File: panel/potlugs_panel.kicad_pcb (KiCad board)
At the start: 2 copper layers, 99 x 91 mm, 819 parts, among them J1 640456-3

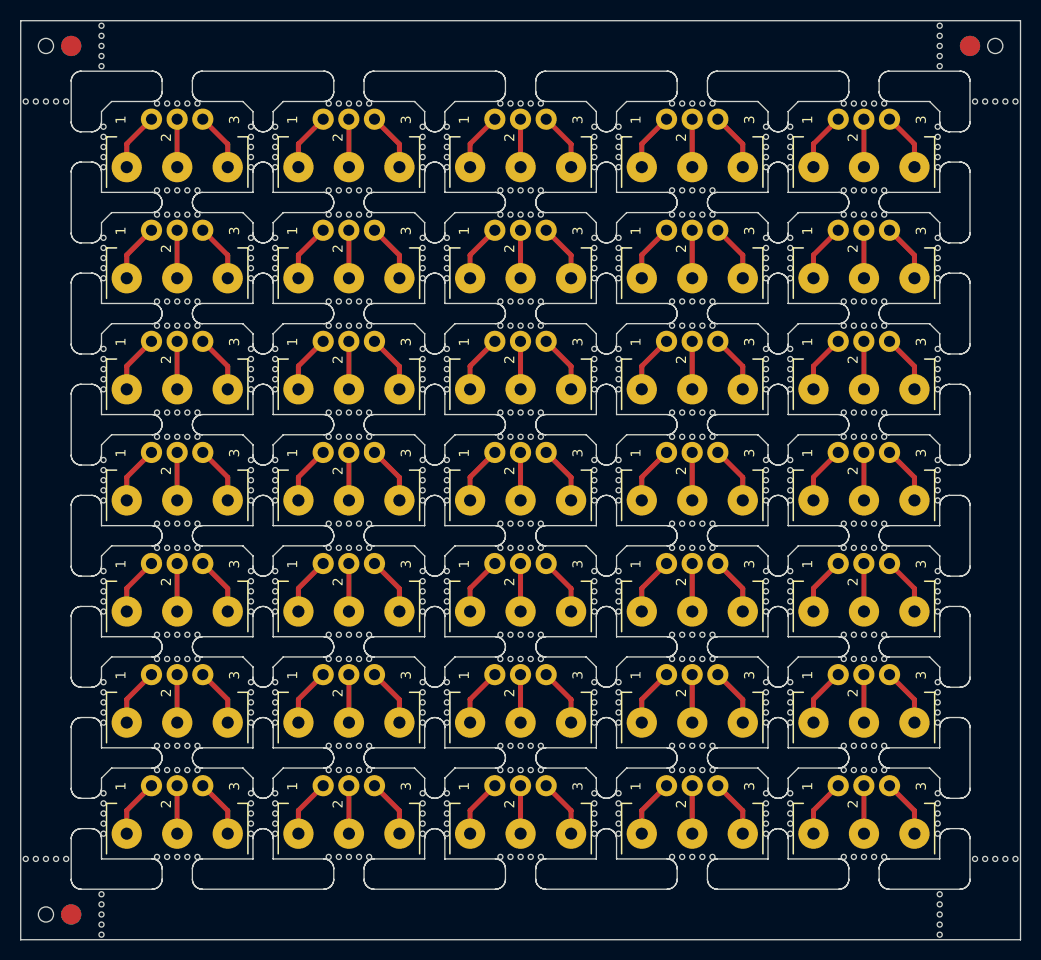
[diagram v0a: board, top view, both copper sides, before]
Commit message: Update panel layout for cost savings.
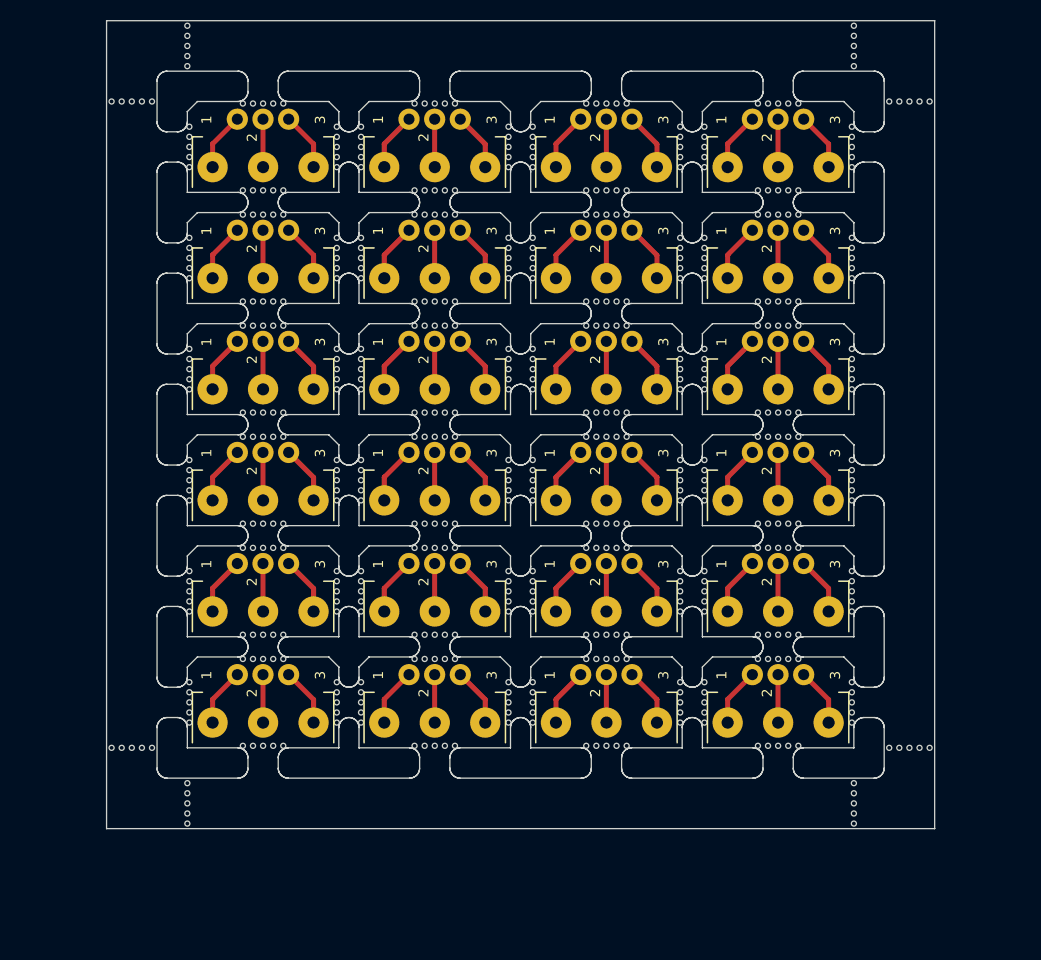
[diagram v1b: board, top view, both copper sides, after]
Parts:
- removed the J1 at (179.9, 62.8)
- removed the J1 at (145.9, 51.8)
- removed the J1 at (179.9, 73.8)
- removed the J1 at (128.9, 40.8)
- removed the J1 at (128.9, 95.8)
- removed the J1 at (128.9, 84.8)
- removed the J1 at (145.9, 95.8)
- removed the J1 at (112.0, 62.8)
- removed the J1 at (162.9, 95.8)
- removed the J1 at (162.9, 84.8)
- removed the J1 at (112.0, 84.8)
- removed the J1 at (179.9, 95.8)
- removed the J1 at (112.0, 51.8)
- removed the J1 at (145.9, 73.8)
- removed the J1 at (145.9, 84.8)
- removed the J1 at (128.9, 62.8)
- removed the J1 at (145.9, 62.8)
- removed the J1 at (128.9, 29.8)
- removed the J1 at (112.0, 29.8)
- removed the J1 at (145.9, 29.8)
- removed the J1 at (179.9, 29.8)
- removed the J1 at (179.9, 84.8)
- removed the J1 at (112.0, 40.8)
- removed the J1 at (162.9, 73.8)
- removed the J1 at (179.9, 40.8)
- removed the J1 at (128.9, 73.8)
- removed the J1 at (112.0, 95.8)
- removed the J1 at (162.9, 51.8)
- removed the J1 at (162.9, 40.8)
- removed the J1 at (128.9, 51.8)
- removed the J1 at (162.9, 62.8)
- removed the J1 at (179.9, 51.8)
- removed the J1 at (112.0, 73.8)
- removed the J1 at (162.9, 29.8)
- removed the J1 at (145.9, 40.8)
- removed KiKit_FID_B_1, KiKit_FID_B_2, KiKit_FID_B_3, KiKit_FID_T_1, KiKit_FID_T_2, KiKit_FID_T_3: Fiducial, Fiducial
- removed KiKit_MB_100_1, KiKit_MB_101_1, KiKit_MB_102_1, KiKit_MB_103_1, KiKit_MB_104_1, KiKit_MB_105_1, KiKit_MB_105_2, KiKit_MB_105_3, KiKit_MB_105_4, KiKit_MB_105_5, KiKit_MB_106_1, KiKit_MB_106_2, KiKit_MB_106_3, KiKit_MB_106_4, KiKit_MB_106_5, KiKit_MB_107_1, KiKit_MB_107_2, KiKit_MB_107_3, KiKit_MB_107_4, KiKit_MB_107_5, KiKit_MB_108_1, KiKit_MB_108_2, KiKit_MB_108_3, KiKit_MB_108_4, KiKit_MB_108_5, KiKit_MB_109_1, KiKit_MB_109_2, KiKit_MB_109_3, KiKit_MB_109_4, KiKit_MB_109_5, KiKit_MB_110_1, KiKit_MB_110_2, KiKit_MB_110_3, KiKit_MB_110_4, KiKit_MB_110_5, KiKit_MB_111_1, KiKit_MB_111_2, KiKit_MB_111_3, KiKit_MB_111_4, KiKit_MB_111_5, KiKit_MB_112_1, KiKit_MB_112_2, KiKit_MB_112_3, KiKit_MB_112_4, KiKit_MB_112_5, KiKit_MB_113_1, KiKit_MB_113_2, KiKit_MB_113_3, KiKit_MB_113_4, KiKit_MB_113_5, KiKit_MB_114_1, KiKit_MB_114_2, KiKit_MB_114_3, KiKit_MB_114_4, KiKit_MB_114_5, KiKit_MB_115_1, KiKit_MB_115_2, KiKit_MB_115_3, KiKit_MB_115_4, KiKit_MB_115_5, KiKit_MB_116_1, KiKit_MB_116_2, KiKit_MB_116_3, KiKit_MB_116_4, KiKit_MB_116_5, KiKit_MB_117_1, KiKit_MB_117_2, KiKit_MB_117_3, KiKit_MB_117_4, KiKit_MB_117_5, KiKit_MB_118_1, KiKit_MB_118_2, KiKit_MB_118_3, KiKit_MB_118_4, KiKit_MB_118_5, KiKit_MB_119_1, KiKit_MB_119_2, KiKit_MB_119_3, KiKit_MB_119_4, KiKit_MB_119_5, KiKit_MB_120_1, KiKit_MB_120_2, KiKit_MB_120_3, KiKit_MB_120_4, KiKit_MB_120_5, KiKit_MB_121_1, KiKit_MB_121_2, KiKit_MB_121_3, KiKit_MB_121_4, KiKit_MB_121_5, KiKit_MB_122_1, KiKit_MB_122_2, KiKit_MB_122_3, KiKit_MB_122_4, KiKit_MB_122_5, KiKit_MB_123_1, KiKit_MB_123_2, KiKit_MB_123_3, KiKit_MB_123_4, KiKit_MB_123_5, KiKit_MB_124_1, KiKit_MB_124_2, KiKit_MB_124_3, KiKit_MB_124_4, KiKit_MB_124_5, KiKit_MB_125_1, KiKit_MB_125_2, KiKit_MB_125_3, KiKit_MB_125_4, KiKit_MB_125_5, KiKit_MB_126_1, KiKit_MB_126_2, KiKit_MB_126_3, KiKit_MB_126_4, KiKit_MB_126_5, KiKit_MB_127_1, KiKit_MB_127_2, KiKit_MB_127_3, KiKit_MB_127_4, KiKit_MB_127_5, KiKit_MB_128_1, KiKit_MB_128_2, KiKit_MB_128_3, KiKit_MB_128_4, KiKit_MB_128_5, KiKit_MB_129_1, KiKit_MB_129_2, KiKit_MB_129_3, KiKit_MB_129_4, KiKit_MB_129_5, KiKit_MB_130_1, KiKit_MB_130_2, KiKit_MB_130_3, KiKit_MB_130_4, KiKit_MB_130_5, KiKit_MB_131_1, KiKit_MB_131_2, KiKit_MB_131_3, KiKit_MB_131_4, KiKit_MB_131_5, KiKit_MB_132_1, KiKit_MB_132_2, KiKit_MB_132_3, KiKit_MB_132_4, KiKit_MB_132_5, KiKit_MB_133_1, KiKit_MB_133_2, KiKit_MB_133_3, KiKit_MB_133_4, KiKit_MB_133_5, KiKit_MB_134_1, KiKit_MB_134_2, KiKit_MB_134_3, KiKit_MB_134_4, KiKit_MB_134_5, KiKit_MB_135_1, KiKit_MB_135_2, KiKit_MB_135_3, KiKit_MB_135_4, KiKit_MB_135_5, KiKit_MB_136_1, KiKit_MB_136_2, KiKit_MB_136_3, KiKit_MB_136_4, KiKit_MB_136_5, KiKit_MB_137_1, KiKit_MB_137_2, KiKit_MB_137_3, KiKit_MB_137_4, KiKit_MB_137_5, KiKit_MB_138_1, KiKit_MB_138_2, KiKit_MB_138_3, KiKit_MB_138_4, KiKit_MB_138_5, KiKit_MB_139_1, KiKit_MB_139_2, KiKit_MB_139_3, KiKit_MB_139_4, KiKit_MB_139_5, KiKit_MB_140_1, KiKit_MB_140_2, KiKit_MB_140_3, KiKit_MB_140_4, KiKit_MB_140_5, KiKit_MB_141_2, KiKit_MB_141_3, KiKit_MB_141_4, KiKit_MB_141_5, KiKit_MB_141_6, KiKit_MB_142_2, KiKit_MB_142_3, KiKit_MB_142_4, KiKit_MB_142_5, KiKit_MB_142_6, KiKit_MB_143_2, KiKit_MB_143_3, KiKit_MB_143_4, KiKit_MB_143_5, KiKit_MB_143_6, KiKit_MB_144_2, KiKit_MB_144_3, KiKit_MB_144_4, KiKit_MB_144_5, KiKit_MB_144_6, KiKit_MB_145_2, KiKit_MB_145_3, KiKit_MB_145_4, KiKit_MB_145_5, KiKit_MB_145_6, KiKit_MB_146_2, KiKit_MB_146_3, KiKit_MB_146_4, KiKit_MB_146_5, KiKit_MB_146_6, KiKit_MB_147_2, KiKit_MB_147_3, KiKit_MB_147_4, KiKit_MB_147_5, KiKit_MB_147_6, KiKit_MB_148_2, KiKit_MB_148_3, KiKit_MB_148_4, KiKit_MB_148_5, KiKit_MB_148_6, KiKit_MB_97_1, KiKit_MB_98_1, KiKit_MB_99_1, KiKit_TO_1, KiKit_TO_2, KiKit_TO_3: NPTH, NPTH
- removed the RV1 at (126.5, 34.5)
- removed the RV1 at (143.5, 89.5)
- removed the RV1 at (160.5, 67.5)
- removed the RV1 at (160.5, 78.5)
- removed the RV1 at (109.5, 78.5)
- removed the RV1 at (109.5, 89.5)
- removed the RV1 at (126.5, 89.5)
- removed the RV1 at (126.5, 78.5)
- removed the RV1 at (143.5, 45.5)
- removed the RV1 at (160.5, 56.5)
- removed the RV1 at (109.5, 34.5)
- removed the RV1 at (126.5, 100.5)
- removed the RV1 at (143.5, 34.5)
- removed the RV1 at (126.5, 45.5)
- removed the RV1 at (177.5, 34.5)
- removed the RV1 at (160.5, 34.5)
- removed the RV1 at (109.5, 45.5)
- removed the RV1 at (143.5, 56.5)
- removed the RV1 at (126.5, 56.5)
- removed the RV1 at (160.5, 45.5)
- removed the RV1 at (177.5, 56.5)
- removed the RV1 at (109.5, 56.5)
- removed the RV1 at (177.5, 67.5)
- removed the RV1 at (177.5, 78.5)
- removed the RV1 at (177.5, 45.5)
- removed the RV1 at (177.5, 100.5)
- removed the RV1 at (109.5, 100.5)
- removed the RV1 at (177.5, 89.5)
- removed the RV1 at (126.5, 67.5)
- removed the RV1 at (160.5, 89.5)
- removed the RV1 at (160.5, 100.5)
- removed the RV1 at (143.5, 100.5)
- removed the RV1 at (109.5, 67.5)
- removed the RV1 at (143.5, 67.5)
- removed the RV1 at (143.5, 78.5)
- added J1: 640456-3, digikey-footprints:PinHeader_1x3_P2.54_Drill1.1mm, F.Cu at (137.4, 84.8)
- added J1: 640456-3, digikey-footprints:PinHeader_1x3_P2.54_Drill1.1mm, F.Cu at (154.4, 84.8)
- added J1: 640456-3, digikey-footprints:PinHeader_1x3_P2.54_Drill1.1mm, F.Cu at (154.4, 73.8)
- added J1: 640456-3, digikey-footprints:PinHeader_1x3_P2.54_Drill1.1mm, F.Cu at (154.4, 29.8)
- added J1: 640456-3, digikey-footprints:PinHeader_1x3_P2.54_Drill1.1mm, F.Cu at (120.5, 73.8)
- added J1: 640456-3, digikey-footprints:PinHeader_1x3_P2.54_Drill1.1mm, F.Cu at (154.4, 51.8)
- added J1: 640456-3, digikey-footprints:PinHeader_1x3_P2.54_Drill1.1mm, F.Cu at (137.4, 40.8)
- added J1: 640456-3, digikey-footprints:PinHeader_1x3_P2.54_Drill1.1mm, F.Cu at (137.4, 73.8)
- added J1: 640456-3, digikey-footprints:PinHeader_1x3_P2.54_Drill1.1mm, F.Cu at (154.4, 62.8)
- added J1: 640456-3, digikey-footprints:PinHeader_1x3_P2.54_Drill1.1mm, F.Cu at (171.4, 40.8)
- added J1: 640456-3, digikey-footprints:PinHeader_1x3_P2.54_Drill1.1mm, F.Cu at (120.5, 40.8)
- added J1: 640456-3, digikey-footprints:PinHeader_1x3_P2.54_Drill1.1mm, F.Cu at (120.5, 62.8)
- added J1: 640456-3, digikey-footprints:PinHeader_1x3_P2.54_Drill1.1mm, F.Cu at (120.5, 29.8)
- added J1: 640456-3, digikey-footprints:PinHeader_1x3_P2.54_Drill1.1mm, F.Cu at (137.4, 62.8)
- added J1: 640456-3, digikey-footprints:PinHeader_1x3_P2.54_Drill1.1mm, F.Cu at (120.5, 51.8)
- added J1: 640456-3, digikey-footprints:PinHeader_1x3_P2.54_Drill1.1mm, F.Cu at (171.4, 73.8)
- added J1: 640456-3, digikey-footprints:PinHeader_1x3_P2.54_Drill1.1mm, F.Cu at (137.4, 51.8)
- added J1: 640456-3, digikey-footprints:PinHeader_1x3_P2.54_Drill1.1mm, F.Cu at (171.4, 29.8)
- added J1: 640456-3, digikey-footprints:PinHeader_1x3_P2.54_Drill1.1mm, F.Cu at (120.5, 84.8)
- added J1: 640456-3, digikey-footprints:PinHeader_1x3_P2.54_Drill1.1mm, F.Cu at (137.4, 29.8)
- added J1: 640456-3, digikey-footprints:PinHeader_1x3_P2.54_Drill1.1mm, F.Cu at (171.4, 51.8)
- added J1: 640456-3, digikey-footprints:PinHeader_1x3_P2.54_Drill1.1mm, F.Cu at (171.4, 62.8)
- added J1: 640456-3, digikey-footprints:PinHeader_1x3_P2.54_Drill1.1mm, F.Cu at (171.4, 84.8)
- added J1: 640456-3, digikey-footprints:PinHeader_1x3_P2.54_Drill1.1mm, F.Cu at (154.4, 40.8)
- added KiKit_MB_100_6: NPTH, NPTH, F.Cu at (181.5, 99.5)
- added KiKit_MB_101_6: NPTH, NPTH, F.Cu at (112.0, 28.0)
- added KiKit_MB_102_6: NPTH, NPTH, F.Cu at (112.0, 92.0)
- added KiKit_MB_103_6: NPTH, NPTH, F.Cu at (189.0, 28.0)
- added KiKit_MB_104_6: NPTH, NPTH, F.Cu at (189.0, 92.0)
- added KiKit_MB_97_6: NPTH, NPTH, F.Cu at (115.5, 24.5)
- added KiKit_MB_98_6: NPTH, NPTH, F.Cu at (181.5, 24.5)
- added KiKit_MB_99_6: NPTH, NPTH, F.Cu at (115.5, 99.5)
- added RV1: R_Potentiometer, Potentiometer_THT:Potentiometer_Alps_RK163_Single_Horizontal, F.Cu at (135.0, 56.5)
- added RV1: R_Potentiometer, Potentiometer_THT:Potentiometer_Alps_RK163_Single_Horizontal, F.Cu at (135.0, 45.5)
- added RV1: R_Potentiometer, Potentiometer_THT:Potentiometer_Alps_RK163_Single_Horizontal, F.Cu at (169.0, 78.5)
- added RV1: R_Potentiometer, Potentiometer_THT:Potentiometer_Alps_RK163_Single_Horizontal, F.Cu at (135.0, 34.5)
- added RV1: R_Potentiometer, Potentiometer_THT:Potentiometer_Alps_RK163_Single_Horizontal, F.Cu at (135.0, 89.5)
- added RV1: R_Potentiometer, Potentiometer_THT:Potentiometer_Alps_RK163_Single_Horizontal, F.Cu at (152.0, 34.5)
- added RV1: R_Potentiometer, Potentiometer_THT:Potentiometer_Alps_RK163_Single_Horizontal, F.Cu at (118.0, 34.5)
- added RV1: R_Potentiometer, Potentiometer_THT:Potentiometer_Alps_RK163_Single_Horizontal, F.Cu at (118.0, 45.5)
- added RV1: R_Potentiometer, Potentiometer_THT:Potentiometer_Alps_RK163_Single_Horizontal, F.Cu at (152.0, 89.5)
- added RV1: R_Potentiometer, Potentiometer_THT:Potentiometer_Alps_RK163_Single_Horizontal, F.Cu at (152.0, 56.5)
- added RV1: R_Potentiometer, Potentiometer_THT:Potentiometer_Alps_RK163_Single_Horizontal, F.Cu at (169.0, 89.5)
- added RV1: R_Potentiometer, Potentiometer_THT:Potentiometer_Alps_RK163_Single_Horizontal, F.Cu at (152.0, 67.5)
- added RV1: R_Potentiometer, Potentiometer_THT:Potentiometer_Alps_RK163_Single_Horizontal, F.Cu at (135.0, 78.5)
- added RV1: R_Potentiometer, Potentiometer_THT:Potentiometer_Alps_RK163_Single_Horizontal, F.Cu at (118.0, 89.5)
- added RV1: R_Potentiometer, Potentiometer_THT:Potentiometer_Alps_RK163_Single_Horizontal, F.Cu at (118.0, 56.5)
- added RV1: R_Potentiometer, Potentiometer_THT:Potentiometer_Alps_RK163_Single_Horizontal, F.Cu at (118.0, 67.5)
- added RV1: R_Potentiometer, Potentiometer_THT:Potentiometer_Alps_RK163_Single_Horizontal, F.Cu at (135.0, 67.5)
- added RV1: R_Potentiometer, Potentiometer_THT:Potentiometer_Alps_RK163_Single_Horizontal, F.Cu at (169.0, 34.5)
- added RV1: R_Potentiometer, Potentiometer_THT:Potentiometer_Alps_RK163_Single_Horizontal, F.Cu at (118.0, 78.5)
- added RV1: R_Potentiometer, Potentiometer_THT:Potentiometer_Alps_RK163_Single_Horizontal, F.Cu at (169.0, 56.5)
- added RV1: R_Potentiometer, Potentiometer_THT:Potentiometer_Alps_RK163_Single_Horizontal, F.Cu at (152.0, 78.5)
- added RV1: R_Potentiometer, Potentiometer_THT:Potentiometer_Alps_RK163_Single_Horizontal, F.Cu at (169.0, 45.5)
- added RV1: R_Potentiometer, Potentiometer_THT:Potentiometer_Alps_RK163_Single_Horizontal, F.Cu at (169.0, 67.5)
- added RV1: R_Potentiometer, Potentiometer_THT:Potentiometer_Alps_RK163_Single_Horizontal, F.Cu at (152.0, 45.5)
- moved KiKit_MB_103_2 90.3 mm to (185.0, 28.0)
- moved KiKit_MB_103_3 90.3 mm to (186.0, 28.0)
- moved KiKit_MB_103_4 90.3 mm to (187.0, 28.0)
- moved KiKit_MB_103_5 90.3 mm to (188.0, 28.0)
- moved KiKit_MB_97_2 82.5 mm to (115.5, 20.5)
- moved KiKit_MB_97_3 81.2 mm to (115.5, 21.5)
- moved KiKit_MB_97_4 79.8 mm to (115.5, 22.5)
- moved KiKit_MB_97_5 78.5 mm to (115.5, 23.5)
- moved KiKit_MB_104_5 75.5 mm to (188.0, 92.0)
- moved KiKit_MB_99_5 73.8 mm to (115.5, 98.5)
- moved KiKit_MB_104_4 73.5 mm to (187.0, 92.0)
- moved KiKit_MB_99_4 72.6 mm to (115.5, 97.5)
- moved KiKit_MB_104_3 71.5 mm to (186.0, 92.0)
- moved KiKit_MB_99_3 71.3 mm to (115.5, 96.5)
- moved KiKit_MB_99_2 70.0 mm to (115.5, 95.5)
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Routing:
- net Board_34-Net-(J1-Pad3): track 5.77 -> 0.00 mm
- net Board_33-Net-(J1-Pad3): track 5.77 -> 0.00 mm
- net Board_32-Net-(J1-Pad3): track 5.77 -> 0.00 mm
- net Board_31-Net-(J1-Pad3): track 5.77 -> 0.00 mm
- net Board_30-Net-(J1-Pad3): track 5.77 -> 0.00 mm
- net Board_29-Net-(J1-Pad3): track 5.77 -> 0.00 mm
- net Board_28-Net-(J1-Pad3): track 5.77 -> 0.00 mm
- net Board_27-Net-(J1-Pad3): track 5.77 -> 0.00 mm
- net Board_26-Net-(J1-Pad3): track 5.77 -> 0.00 mm
- net Board_25-Net-(J1-Pad3): track 5.77 -> 0.00 mm
- net Board_24-Net-(J1-Pad3): track 5.77 -> 0.00 mm
- net Board_30-Net-(J1-Pad1): track 5.76 -> 0.00 mm
- net Board_25-Net-(J1-Pad1): track 5.76 -> 0.00 mm
- net Board_34-Net-(J1-Pad1): track 5.76 -> 0.00 mm
- net Board_33-Net-(J1-Pad1): track 5.76 -> 0.00 mm
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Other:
- board size 99 x 91 mm -> 82 x 80 mm
